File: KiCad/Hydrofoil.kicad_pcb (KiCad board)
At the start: 2 copper layers, 219.6 x 35 mm, 62 parts, among them J1 Conn_01x03_Pin, J2 Conn_01x03_Pin, Q1 BSS138, Q2 BSS138, Q3 BSS138, Q4 BSS138, Q5 BSS138, U1 ESP32-C3-MINI-1-N4, U2 LD1117S33CTR, U3 TPS22917DBV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

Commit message: Add MPN to BOM, create PCBWay specific fabrication files
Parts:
- CR1, CR2, CR3, CR4: value CUS08F30_H3FT -> CUS08F30_H3F

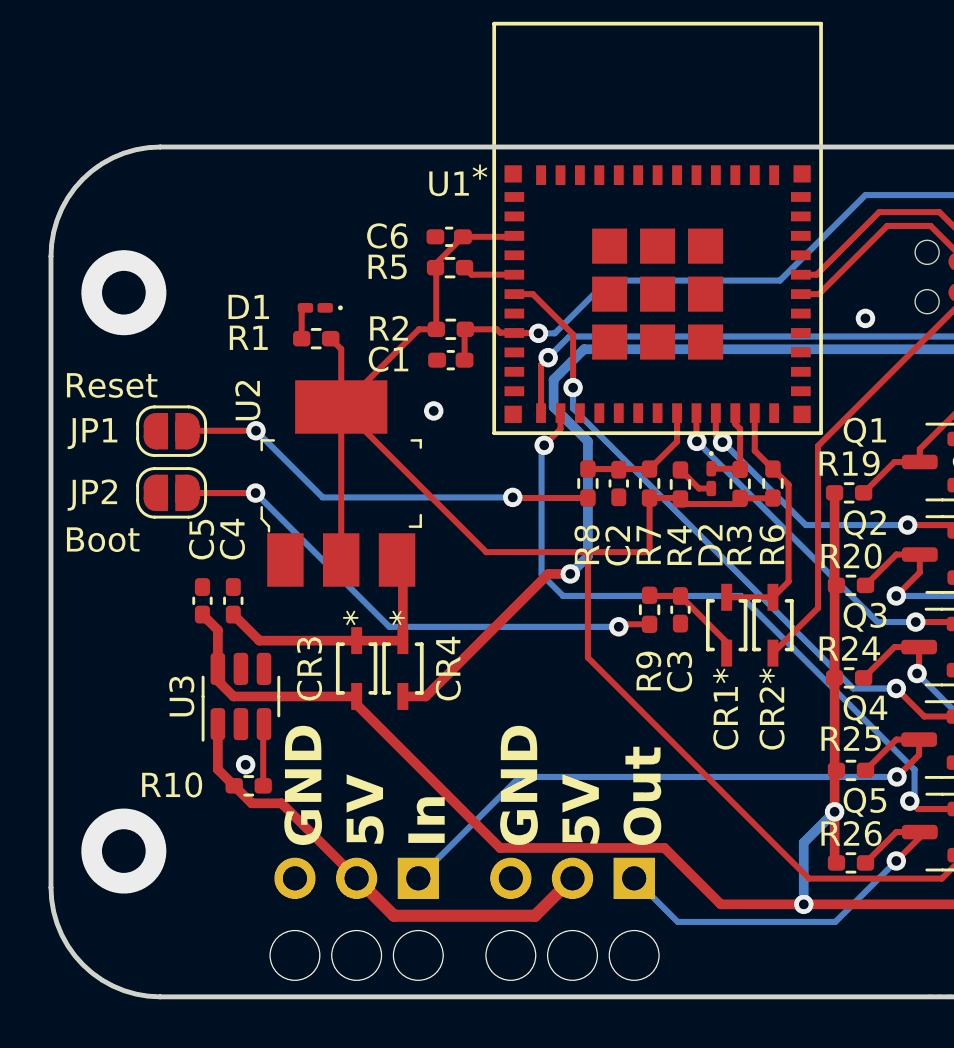
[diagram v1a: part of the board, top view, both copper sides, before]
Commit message: Widen servo traces, add C to slikscreen, replace LEDs to 0402
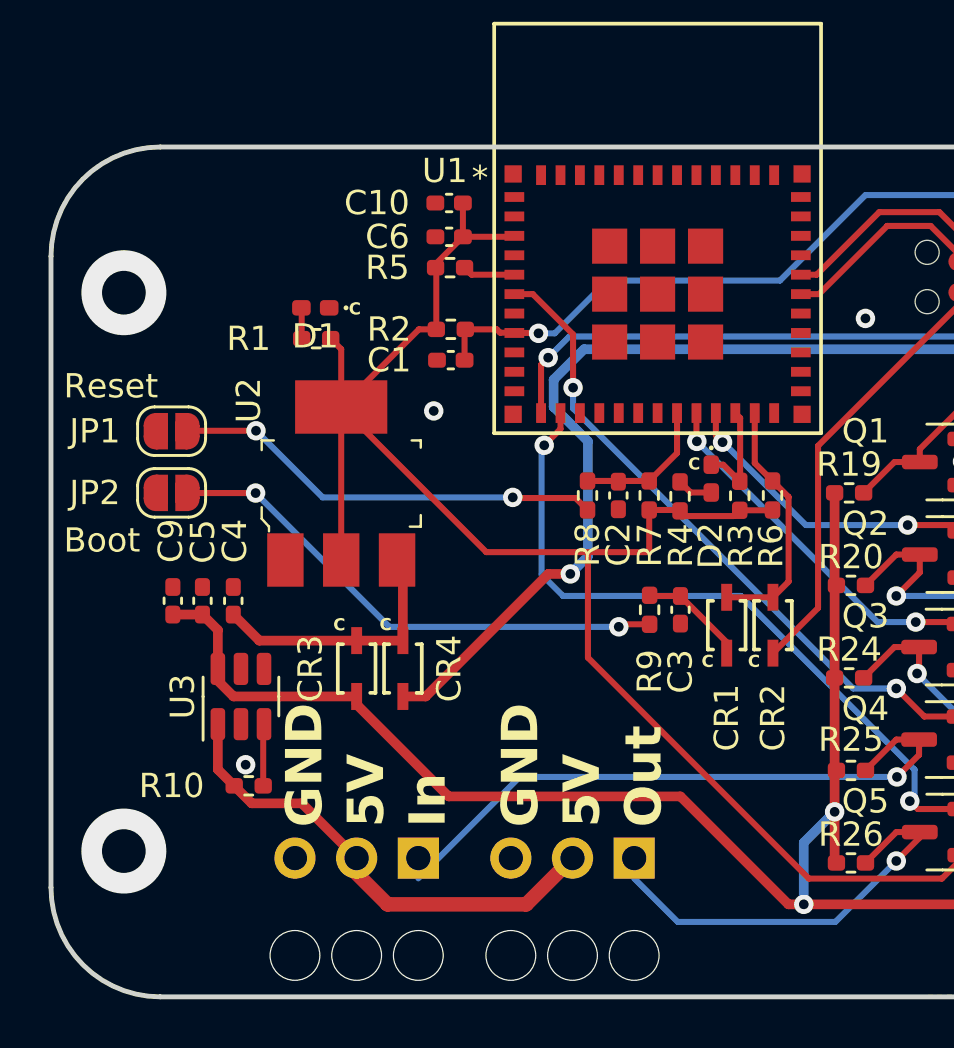
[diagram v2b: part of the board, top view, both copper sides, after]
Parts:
- added C10: 10u, Capacitor_SMD:C_0402_1005Metric_Pad0.74x0.62mm_HandSolder, F.Cu at (55.2, 74.0)
- added C9: 10u, Capacitor_SMD:C_0402_1005Metric_Pad0.74x0.62mm_HandSolder, F.Cu at (43.9, 90.4)
- D1: value Green -> Yellow; footprint LED_SMD:LED_0201_0603Metric_Pad0.64x0.40mm_HandSolder -> LED_SMD:LED_0402_1005Metric_Pad0.77x0.64mm_HandSolder
- D2: footprint LED_SMD:LED_0201_0603Metric_Pad0.64x0.40mm_HandSolder -> LED_SMD:LED_0402_1005Metric_Pad0.77x0.64mm_HandSolder
- moved J1 0.83 mm to (51.4, 101.0)
- moved J2 0.83 mm to (60.3, 101.0)
- moved R4 0.49 mm to (64.8, 86.1)
- moved R6 0.49 mm to (68.6, 86.0)
- moved R7 0.49 mm to (63.5, 86.0)
- moved R8 0.49 mm to (60.9, 86.0)
- moved C2 0.49 mm to (62.2, 86.0)
- moved R3 0.49 mm to (67.2, 86.0)
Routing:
- net +5V: track 66.7 -> 67.9 mm
- net +3.3V: track 104.7 -> 105.6 mm
- net User-LED: track 3.66 -> 4.42 mm
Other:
- board text added: "C"

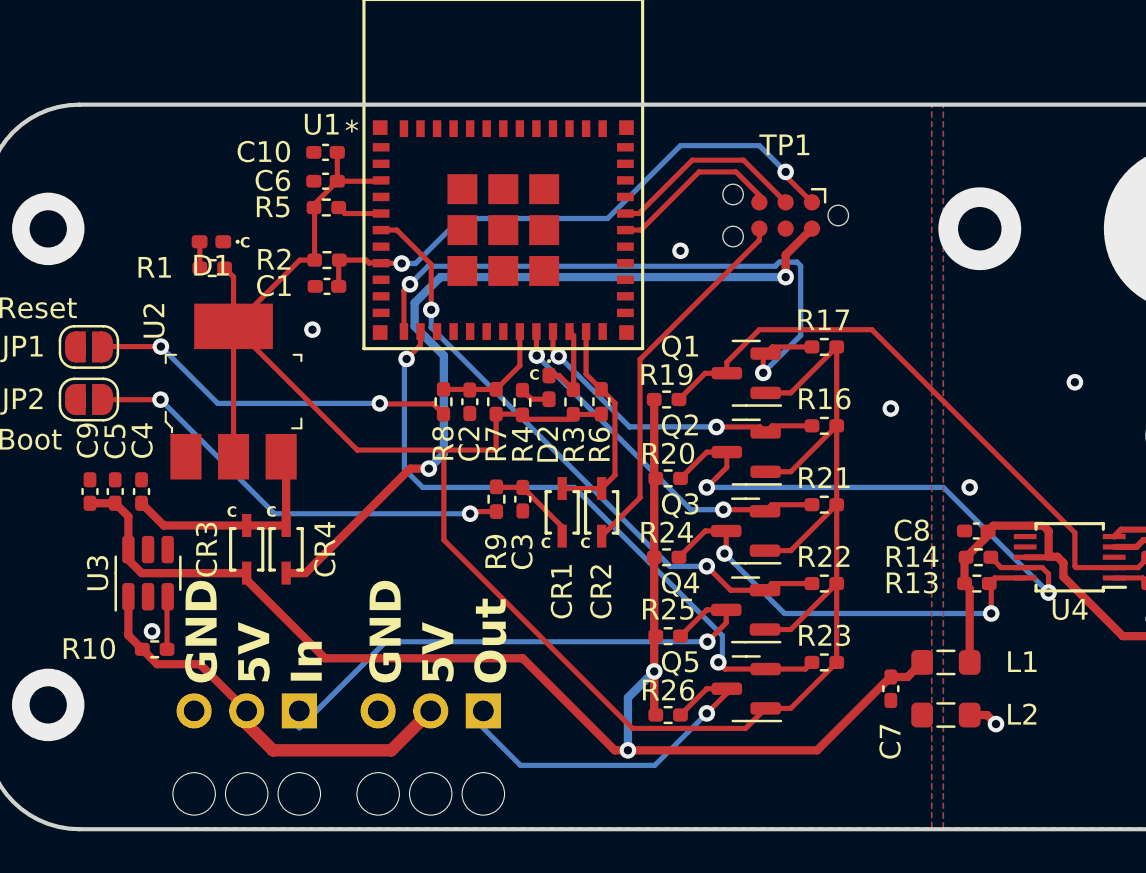
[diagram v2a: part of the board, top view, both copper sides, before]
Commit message: Add missing silkscreen texts
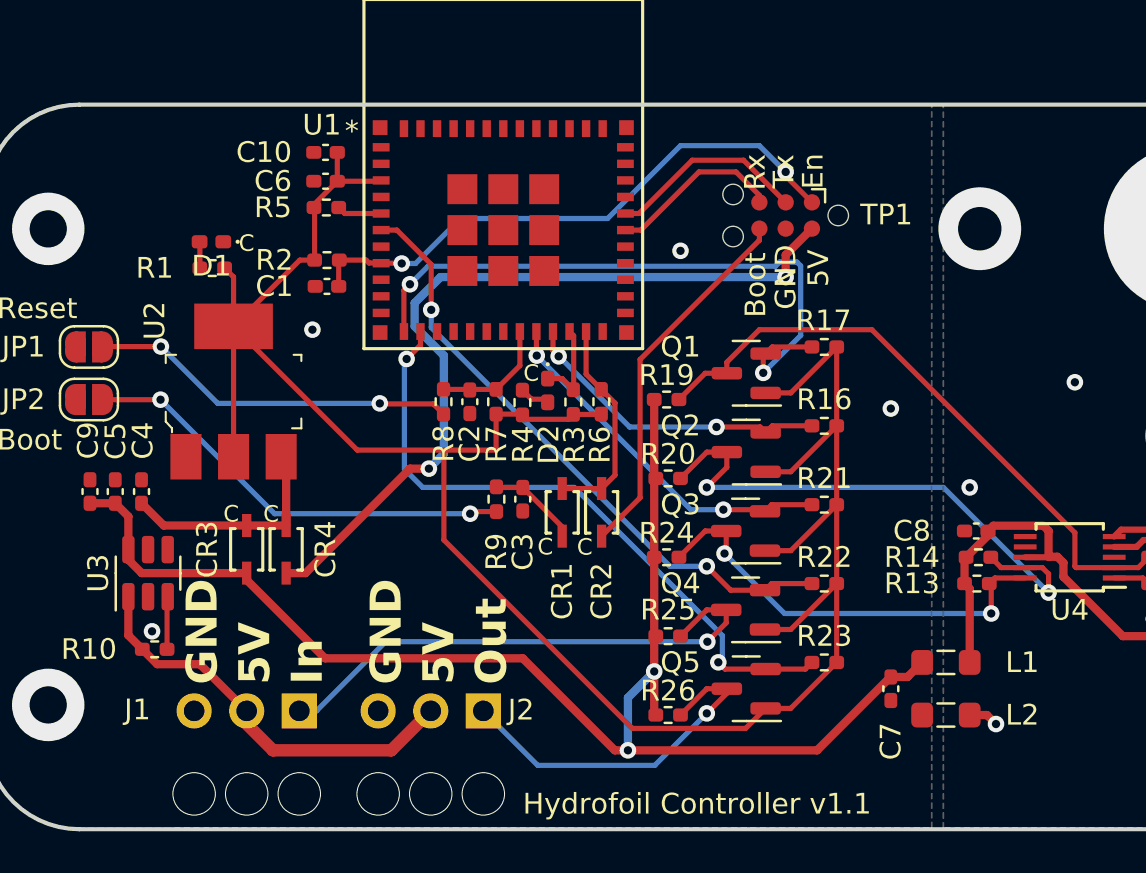
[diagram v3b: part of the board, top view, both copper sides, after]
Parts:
- moved D2 0.16 mm to (66.0, 85.5)
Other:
- board text added: "En"
- board text added: "Hydrofoil Controller v1.1"
- board text added: "J1"
- board text added: "J2"
- board text added: "Rx"
- board text added: "Tx"
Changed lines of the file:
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@@
   (net 59 "unconnected-(U3-QOD-Pad5)")
   (footprint "LED_SMD:LED_0402_1005Metric_Pad0.77x0.64mm_HandSolder" (layer "F.Cu")
-    (at 66.04 85.336627 -90)
+    (at 65.973709 85.486279 -90)
     (descr "LED SMD 0402 (1005 Metric), square (rectangular) end terminal, IPC_7351 nominal, (Body size source: http://www.tortai-tech.com/upload/download/2011102023233369053.pdf), generated with kicad-footprint-generator")
     (tags "LED handsolder")
@@
     (property "ki_keywords" "LED diode")
     (attr smd)
-    (fp_text reference "D2" (at 2.763125 0.031507 -90) (layer "F.SilkS")
+    (fp_text reference "D2" (at 2.612595 -0.051572 -90) (layer "F.SilkS")
         (effects (font (size 1 1) (thickness 0.15)))
     )
@@
     (property "exclude_from_bom" "")
     (attr exclude_from_pos_files exclude_from_bom)
-    (fp_text reference "TP1" (at 0 3.374127) (layer "F.SilkS")
+    (fp_text reference "TP1" (at -4.869591 0.034831) (layer "F.SilkS")
         (effects (font (size 1 1) (thickness 0.15)))
     )
@@
     (effects (font (size 1.5 1.5) (thickness 0.3) bold) (justify left bottom))
   )
-  (gr_text "C" (at 51.109365 78.63746) (layer "F.SilkS")
-    (effects (font (size 0.5 0.5) (thickness 0.1) bold) (justify left bottom))
+  (gr_text "5V" (at 79.640585 80.488997 90) (layer "F.SilkS")
+    (effects (font (size 1 1) (thickness 0.15)) (justify left bottom))
+  )
+  (gr_text "C" (at 50.301648 91.917203) (layer "F.SilkS")
+    (effects (font (size 0.8 0.8) (thickness 0.12)) (justify left bottom))
   )
-  (gr_text "C" (at 65.083495 85.02389) (layer "F.SilkS")
-    (effects (font (size 0.5 0.5) (thickness 0.1) bold) (justify left bottom))
+  (gr_text "GND" (at 78.060578 81.583805 90) (layer "F.SilkS")
+    (effects (font (size 1 1) (thickness 0.15)) (justify left bottom))
+  )
+  (gr_text "Tx" (at 77.96105 75.724093 90) (layer "F.SilkS")
+    (effects (font (size 1 1) (thickness 0.15)) (justify left bottom))
+  )
+  (gr_text "Hydrofoil Controller v1.1" (at 64.77 106.045) (layer "F.SilkS")
+    (effects (font (size 1 1) (thickness 0.15)) (justify left bottom))
+  )
+  (gr_text "C" (at 64.794256 85.119188) (layer "F.SilkS")
+    (effects (font (size 0.8 0.8) (thickness 0.12)) (justify left bottom))
   )
   (gr_text "5V" (at 61.595 99.695 90) (layer "F.SilkS")
     (effects (font (size 1.5 1.5) (thickness 0.3) bold) (justify left bottom))
   )
+  (gr_text "J2" (at 64.051414 101.50175) (layer "F.SilkS")
+    (effects (font (size 1 1) (thickness 0.15)) (justify left bottom))
+  )
+  (gr_text "Boot" (at 76.60498 81.969476 90) (layer "F.SilkS")
+    (effects (font (size 1 1) (thickness 0.15)) (justify left bottom))
+  )
   (gr_text "GND" (at 50.165 99.695 90) (layer "F.SilkS")
     (effects (font (size 1.5 1.5) (thickness 0.3) bold) (justify left bottom))
@@
     (effects (font (size 1 1) (thickness 0.15)) (justify left bottom))
   )
-  (gr_text "C" (at 65.637609 93.154264) (layer "F.SilkS")
-    (effects (font (size 0.5 0.5) (thickness 0.1) bold) (justify left bottom))
+  (gr_text "Rx" (at 76.580098 75.823621 90) (layer "F.SilkS")
+    (effects (font (size 1 1) (thickness 0.15)) (justify left bottom))
   )
-  (gr_text "C" (at 50.470167 91.64638) (layer "F.SilkS")
-    (effects (font (size 0.5 0.5) (thickness 0.1) bold) (justify left bottom))
+  (gr_text "En" (at 79.375 75.764127 90) (layer "F.SilkS")
+    (effects (font (size 1 1) (thickness 0.15)) (justify left bottom))
+  )
+  (gr_text "C" (at 52.229329 91.925103) (layer "F.SilkS")
+    (effects (font (size 0.8 0.8) (thickness 0.12)) (justify left bottom))
+  )
+  (gr_text "C" (at 65.474233 93.506815) (layer "F.SilkS")
+    (effects (font (size 0.8 0.8) (thickness 0.12)) (justify left bottom))
+  )
+  (gr_text "J1" (at 45.518299 101.492445) (layer "F.SilkS")
+    (effects (font (size 1 1) (thickness 0.15)) (justify left bottom))
   )
-  (gr_text "C" (at 52.375325 91.639788) (layer "F.SilkS")
-    (effects (font (size 0.5 0.5) (thickness 0.1) bold) (justify left bottom))
+  (gr_text "C" (at 67.380846 93.517349) (layer "F.SilkS")
+    (effects (font (size 0.8 0.8) (thickness 0.12)) (justify left bottom))
   )
   (gr_text "GND" (at 59.055 99.695 90) (layer "F.SilkS")
     (effects (font (size 1.5 1.5) (thickness 0.3) bold) (justify left bottom))
   )
-  (gr_text "C" (at 67.545997 93.153714) (layer "F.SilkS")
-    (effects (font (size 0.5 0.5) (thickness 0.1) bold) (justify left bottom))
+  (gr_text "C" (at 51.045705 78.841826) (layer "F.SilkS")
+    (effects (font (size 0.8 0.8) (thickness 0.12)) (justify left bottom))
   )
   (via (at 255.318605 98.686961) (size 0.8) (drill 0.4) (layers "F.Cu" "B.Cu") (free) (net 0))
@@
   (segment (start 49.1725 78.456627) (end 49.325 78.304127) (width 0.25) (layer "F.Cu") (net 13))
   (segment (start 49.1725 79.574127) (end 49.1725 78.456627) (width 0.25) (layer "F.Cu") (net 13))
-  (segment (start 66.529548 84.764127) (end 67.212613 85.447192) (width 0.25) (layer "F.Cu") (net 14))
-  (segment (start 66.04 84.764127) (end 66.529548 84.764127) (width 0.25) (layer "F.Cu") (net 14))
   (segment (start 67.229705 85.4301) (end 67.229705 82.838834) (width 0.25) (layer "F.Cu") (net 14))
+  (segment (start 66.6792 84.913779) (end 67.212613 85.447192) (width 0.25) (layer "F.Cu") (net 14))
+  (segment (start 65.973709 84.913779) (end 66.6792 84.913779) (width 0.25) (layer "F.Cu") (net 14))
   (segment (start 67.212613 85.447192) (end 67.229705 85.4301) (width 0.25) (layer "F.Cu") (net 14))
   (segment (start 67.229705 82.838834) (end 67.029998 82.639127) (width 0.25) (layer "F.Cu") (net 14))
@@
   (segment (start 73.66 96.084127) (end 72.39 97.354127) (width 0.25) (layer "F.Cu") (net 23))
   (via (at 73.687551 97.623755) (size 0.8) (drill 0.4) (layers "F.Cu" "B.Cu") (net 23))
-  (segment (start 58.150372 97.623755) (end 53.975 101.799127) (width 0.25) (layer "B.Cu") (net 23))
+  (segment (start 54.809127 100.965) (end 53.975 100.965) (width 0.25) (layer "B.Cu") (net 23))
   (segment (start 73.687551 97.623755) (end 58.150372 97.623755) (width 0.25) (layer "B.Cu") (net 23))
+  (segment (start 58.150372 97.623755) (end 54.809127 100.965) (width 0.25) (layer "B.Cu") (net 23))
   (segment (start 59.160094 83.965431) (end 59.829999 83.295527) (width 0.25) (layer "F.Cu") (net 24))
   (segment (start 76.5025 98.944127) (end 74.541264 98.944127) (width 0.25) (layer "F.Cu") (net 24))
@@
   (segment (start 74.6275 99.894127) (end 74.6275 100.117127) (width 0.25) (layer "F.Cu") (net 25))
   (via (at 73.66 101.084627) (size 0.8) (drill 0.4) (layers "F.Cu" "B.Cu") (net 25))
-  (segment (start 71.149627 103.595) (end 64.660873 103.595) (width 0.25) (layer "B.Cu") (net 25))
-  (segment (start 64.660873 103.595) (end 62.865 101.799127) (width 0.25) (layer "B.Cu") (net 25))
+  (segment (start 71.149627 103.595) (end 65.495 103.595) (width 0.25) (layer "B.Cu") (net 25))
+  (segment (start 65.495 103.595) (end 62.865 100.965) (width 0.25) (layer "B.Cu") (net 25))
   (segment (start 73.66 101.084627) (end 71.149627 103.595) (width 0.25) (layer "B.Cu") (net 25))
   (segment (start 45.72 97.316627) (end 45.72 95.449127) (width 0.4) (layer "F.Cu") (net 26))
